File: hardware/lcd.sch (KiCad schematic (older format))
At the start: 3 parts

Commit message: Im Schaltplan die Debug LED mit Vorwiderstand durch einen PIN Header ersetz für eventuelle Erweiterung. Auf Revision 1.3 gesetzt
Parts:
- renumbered R11 to R10
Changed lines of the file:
@@
 Sheet 3 4
 Title "1541-rebuid"
-Date "2018-05-04"
-Rev "1.2.1"
+Date "2018-05-05"
+Rev "1.3"
 Comp ""
 Comment1 "Erstellt: von: Thorsten Kattanek"
@@
 	6850 3350 6850 3500
 $Comp
-L GND #PWR20
+L GND #PWR19
 U 1 1 55F9D0E8
 P 6850 3500
-F 0 "#PWR20" H 6850 3250 50  0001 C CNN
+F 0 "#PWR19" H 6850 3250 50  0001 C CNN
 F 1 "GND" H 6850 3350 50  0000 C CNN
 F 2 "" H 6850 3500 60  0000 C CNN
@@
 Connection ~ 5750 3400
 $Comp
-L +5V #PWR18
+L +5V #PWR17
 U 1 1 55F9F555
 P 5450 3500
-F 0 "#PWR18" H 5450 3350 50  0001 C CNN
+F 0 "#PWR17" H 5450 3350 50  0001 C CNN
 F 1 "+5V" H 5450 3640 50  0000 C CNN
 F 2 "" H 5450 3500 60  0000 C CNN
@@
 	5550 3750 5550 3350
 $Comp
-L +5V #PWR17
+L +5V #PWR16
 U 1 1 55F9F9A0
 P 4650 3400
-F 0 "#PWR17" H 4650 3250 50  0001 C CNN
+F 0 "#PWR16" H 4650 3250 50  0001 C CNN
 F 1 "+5V" H 4650 3540 50  0000 C CNN
 F 2 "" H 4650 3400 60  0000 C CNN
@@
 	4650 3400 4750 3400
 $Comp
-L R R11
+L R R10
 U 1 1 55F9FBFA
 P 6750 3850
-F 0 "R11" V 6830 3850 50  0000 C CNN
+F 0 "R10" V 6830 3850 50  0000 C CNN
 F 1 "150" V 6750 3850 50  0000 C CNN
 F 2 "Resistors_ThroughHole:Resistor_Horizontal_RM10mm" V 6680 3850 30  0001 C CNN
@@
 $EndComp
 $Comp
-L +5V #PWR19
+L +5V #PWR18
 U 1 1 55F9FC92
 P 6750 4100
-F 0 "#PWR19" H 6750 3950 50  0001 C CNN
+F 0 "#PWR18" H 6750 3950 50  0001 C CNN
 F 1 "+5V" H 6750 4240 50  0000 C CNN
 F 2 "" H 6750 4100 60  0000 C CNN

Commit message: LCD Display wird nun als 10 PIN Wannenstecker rausgeführt. PIN Belegung des Steckers wird im Schaltplan beschrieben.
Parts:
- removed DS1: LCD16X2, w_indicators:lcd_20x4, symbol LCD16X2
- added J2: LCD Display, symbol Conn_02x05_Odd_Even
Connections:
- wire segments 23 -> 16
- no-connect marks 4 -> 0
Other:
- note added: "R10 hängt von der Hintergrundbeleuchtung des LCD Displays ab !"
- note added: "Steckerbelegung für das LCD Display (20x4)\n\nPIN_01: VDD(2) ... +5V\nPIN_02: VSS(1), R/W(5), LED-/K(16) ... GND\nPIN_03: D4(11)\nPIN_04: D5(12)\nPIN_05: D6(13)\nPIN_06: D7(14)\nPIN_07: E(6)\nPIN_08: RS(4)\nPIN_09: LED+/A(15)\nPIN_10: VO(3)\n"
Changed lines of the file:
@@
 Title "1541-rebuid"
 Date "2018-05-05"
-Rev "1.3"
+Rev "1.3.1"
 Comp ""
 Comment1 "Erstellt: von: Thorsten Kattanek"
@@
 Comment4 ""
 $EndDescr
-Text HLabel 4700 4000 0    60   Input ~ 0
-D0
-Text HLabel 4700 4100 0    60   Input ~ 0
-D1
-Text HLabel 4700 4200 0    60   Input ~ 0
-D2
-Text HLabel 4700 4300 0    60   Input ~ 0
-D3
-Text HLabel 4700 3800 0    60   Input ~ 0
-RS
-Text HLabel 4700 3900 0    60   Input ~ 0
-EN
-NoConn ~ 5950 3350
-NoConn ~ 6050 3350
-NoConn ~ 6150 3350
-NoConn ~ 6250 3350
-Wire Wire Line
-	4700 4000 6350 4000
-Wire Wire Line
-	6350 4000 6350 3350
-Wire Wire Line
-	4700 4100 6450 4100
-Wire Wire Line
-	6450 4100 6450 3350
-Wire Wire Line
-	4700 4200 6550 4200
-Wire Wire Line
-	6550 4200 6550 3350
-Wire Wire Line
-	4700 4300 6650 4300
-Wire Wire Line
-	6650 4300 6650 3350
-Wire Wire Line
-	4700 3900 5850 3900
-Wire Wire Line
-	5850 3900 5850 3350
-Wire Wire Line
-	4700 3800 5650 3800
-Wire Wire Line
-	5650 3800 5650 3350
-Wire Wire Line
-	5750 3350 5750 3400
-Wire Wire Line
-	5250 3400 6850 3400
-Wire Wire Line
-	6850 3350 6850 3500
 $Comp
-L GND #PWR19
-U 1 1 55F9D0E8
-P 6850 3500
-F 0 "#PWR19" H 6850 3250 50  0001 C CNN
-F 1 "GND" H 6850 3350 50  0000 C CNN
-F 2 "" H 6850 3500 60  0000 C CNN
-F 3 "" H 6850 3500 60  0000 C CNN
-	1    6850 3500
+L Conn_02x05_Odd_Even J2
+U 1 1 5AEE2FA0
+P 5050 3600
+F 0 "J2" H 5100 3900 50  0000 C CNN
+F 1 "LCD Display" H 5100 3300 50  0000 C CNN
+F 2 "" H 5050 3600 50  0001 C CNN
+F 3 "" H 5050 3600 50  0001 C CNN
+	1    5050 3600
+	0    1    1    0
+$EndComp
+Text Notes 5950 4100 0    60   ~ 0
+Steckerbelegung für das LCD Display (20x4)\n\nPIN_01: VDD(2) ... +5V\nPIN_02: VSS(1), R/W(5), LED-/K(16) ... GND\nPIN_03: D4(11)\nPIN_04: D5(12)\nPIN_05: D6(13)\nPIN_06: D7(14)\nPIN_07: E(6)\nPIN_08: RS(4)\nPIN_09: LED+/A(15)\nPIN_10: VO(3)\n
+$Comp
+L +5V #PWR17
+U 1 1 5AEE3573
+P 5250 2450
+F 0 "#PWR17" H 5250 2300 50  0001 C CNN
+F 1 "+5V" H 5250 2590 50  0000 C CNN
+F 2 "" H 5250 2450 60  0000 C CNN
+F 3 "" H 5250 2450 60  0000 C CNN
+	1    5250 2450
 	1    0    0    -1
 $EndComp
-Connection ~ 6850 3400
+Text HLabel 5150 2900 1    60   Input ~ 0
+D0
+Text HLabel 5150 4150 3    60   Input ~ 0
+D1
+Text HLabel 5050 2900 1    60   Input ~ 0
+D2
+Text HLabel 5050 4150 3    60   Input ~ 0
+D3
+Text HLabel 4950 2900 1    60   Input ~ 0
+EN
+Text HLabel 4950 4150 3    60   Input ~ 0
+RS
+Wire Wire Line
+	5250 2450 5250 2550
+Wire Wire Line
+	5250 2550 5250 3400
+Wire Wire Line
+	5150 2900 5150 3400
+Wire Wire Line
+	5150 3900 5150 4150
+Wire Wire Line
+	5050 3400 5050 2900
+Wire Wire Line
+	5050 3900 5050 4150
+Wire Wire Line
+	4950 2900 4950 3400
+Wire Wire Line
+	4950 3900 4950 4150
 $Comp
-L LCD16X2 DS1
-U 1 1 55F9CFCD
-P 6100 2850
-F 0 "DS1" H 5300 3250 40  0000 C CNN
-F 1 "LCD16X2" H 6800 3250 40  0000 C CNN
-F 2 "w_indicators:lcd_20x4" H 6100 2800 35  0000 C CIN
-F 3 "" H 6100 2850 60  0000 C CNN
-	1    6100 2850
+L R R10
+U 1 1 5AEE40E3
+P 4850 3100
+F 0 "R10" V 4930 3100 50  0000 C CNN
+F 1 "150" V 4850 3100 50  0000 C CNN
+F 2 "Resistors_ThroughHole:Resistor_Horizontal_RM10mm" V 4780 3100 30  0001 C CNN
+F 3 "" H 4850 3100 30  0000 C CNN
+	1    4850 3100
+	-1   0    0    1
+$EndComp
+Wire Wire Line
+	4850 2950 4850 2550
+Wire Wire Line
+	4850 2550 5250 2550
+Connection ~ 5250 2550
+Wire Wire Line
+	4850 3250 4850 3400
+$Comp
+L GND #PWR18
+U 1 1 5AEE45C6
+P 5250 4750
+F 0 "#PWR18" H 5250 4500 50  0001 C CNN
+F 1 "GND" H 5250 4600 50  0000 C CNN
+F 2 "" H 5250 4750 60  0000 C CNN
+F 3 "" H 5250 4750 60  0000 C CNN
+	1    5250 4750
 	1    0    0    -1
 $EndComp
 Wire Wire Line
-	5350 3350 5350 3400
-Connection ~ 5750 3400
+	5250 3900 5250 4550
+Wire Wire Line
+	5250 4550 5250 4750
 $Comp
-L +5V #PWR17
-U 1 1 55F9F555
-P 5450 3500
-F 0 "#PWR17" H 5450 3350 50  0001 C CNN
-F 1 "+5V" H 5450 3640 50  0000 C CNN
-F 2 "" H 5450 3500 60  0000 C CNN
-F 3 "" H 5450 3500 60  0000 C CNN
-	1    5450 3500
-	-1   0    0    1
+L POT-RESCUE-1541-rebuild RV1
+U 1 1 5AEE481D
+P 4850 4550
+F 0 "RV1" H 4850 4450 50  0000 C CNN
+F 1 "10k" H 4850 4550 50  0000 C CNN
+F 2 "Potentiometers:Potentiometer_Bourns_3339P_Angular_ScrewUp" H 4850 4550 60  0001 C CNN
+F 3 "" H 4850 4550 60  0000 C CNN
+	1    4850 4550
+	1    0    0    -1
 $EndComp
 Wire Wire Line
-	5450 3350 5450 3500
-$Comp
-L POT-RESCUE-1541-rebuild RV1
-U 1 1 55F9F8C0
-P 5000 3400
-F 0 "RV1" H 5000 3300 50  0000 C CNN
-F 1 "10k" H 5000 3400 50  0000 C CNN
-F 2 "Potentiometers:Potentiometer_Bourns_3339P_Angular_ScrewUp" H 5000 3400 60  0001 C CNN
-F 3 "" H 5000 3400 60  0000 C CNN
-	1    5000 3400
-	-1   0    0    1
-$EndComp
-Connection ~ 5350 3400
+	5100 4550 5250 4550
+Connection ~ 5250 4550
 Wire Wire Line
-	5000 3550 5000 3750
-Wire Wire Line
-	5000 3750 5550 3750
-Wire Wire Line
-	5550 3750 5550 3350
+	4850 3900 4850 4400
 $Comp
 L +5V #PWR16
-U 1 1 55F9F9A0
-P 4650 3400
-F 0 "#PWR16" H 4650 3250 50  0001 C CNN
-F 1 "+5V" H 4650 3540 50  0000 C CNN
-F 2 "" H 4650 3400 60  0000 C CNN
-F 3 "" H 4650 3400 60  0000 C CNN
-	1    4650 3400
+U 1 1 5AEE4960
+P 4350 4550
+F 0 "#PWR16" H 4350 4400 50  0001 C CNN
+F 1 "+5V" H 4350 4690 50  0000 C CNN
+F 2 "" H 4350 4550 60  0000 C CNN
+F 3 "" H 4350 4550 60  0000 C CNN
+	1    4350 4550
 	0    -1   -1   0
 $EndComp
 Wire Wire Line
-	4650 3400 4750 3400
-$Comp
-L R R10
-U 1 1 55F9FBFA
-P 6750 3850
-F 0 "R10" V 6830 3850 50  0000 C CNN
-F 1 "150" V 6750 3850 50  0000 C CNN
-F 2 "Resistors_ThroughHole:Resistor_Horizontal_RM10mm" V 6680 3850 30  0001 C CNN
-F 3 "" H 6750 3850 30  0000 C CNN
-	1    6750 3850
-	1    0    0    -1
-$EndComp
-$Comp
-L +5V #PWR18
-U 1 1 55F9FC92
-P 6750 4100
-F 0 "#PWR18" H 6750 3950 50  0001 C CNN
-F 1 "+5V" H 6750 4240 50  0000 C CNN
-F 2 "" H 6750 4100 60  0000 C CNN
-F 3 "" H 6750 4100 60  0000 C CNN
-	1    6750 4100
-	-1   0    0    1
-$EndComp
-Wire Wire Line
-	6750 3350 6750 3700
-Wire Wire Line
-	6750 4000 6750 4100
+	4350 4550 4600 4550
+Text Notes 650  7600 0    60   ~ 0
+R10 hängt von der Hintergrundbeleuchtung des LCD Displays ab !
 $EndSCHEMATC

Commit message: Im Schaltplan die 3 Steuertasten als 4 PINS (Key1, Key2, Key3 und GND) rausgeführt. Auf Revesion 1.3.2 gesetzt.
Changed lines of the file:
@@
 Sheet 3 4
 Title "1541-rebuid"
-Date "2018-05-05"
-Rev "1.3.1"
+Date "2018-05-06"
+Rev "1.3.2"
 Comp ""
 Comment1 "Erstellt: von: Thorsten Kattanek"
@@
 RS
 Wire Wire Line
-	5250 2450 5250 2550
-Wire Wire Line
-	5250 2550 5250 3400
+	5250 2450 5250 3400
 Wire Wire Line
 	5150 2900 5150 3400
@@
 $EndComp
 Wire Wire Line
-	5250 3900 5250 4550
-Wire Wire Line
-	5250 4550 5250 4750
+	5250 3900 5250 4750
 $Comp
 L POT-RESCUE-1541-rebuild RV1

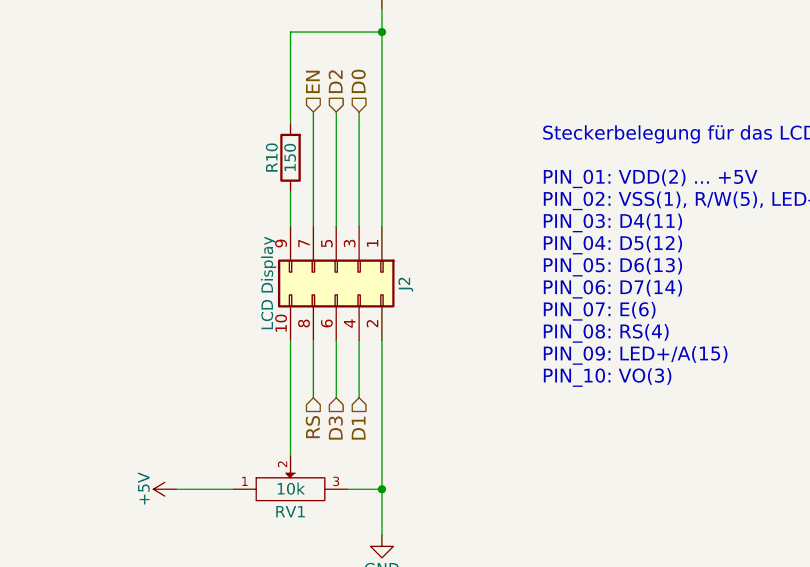
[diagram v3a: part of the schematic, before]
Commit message: Jumper für EXT_5V hinzugefügt. Schaltplan aufgeräumt. Schaltplan auf Revision 1.3.3 gesetzt.
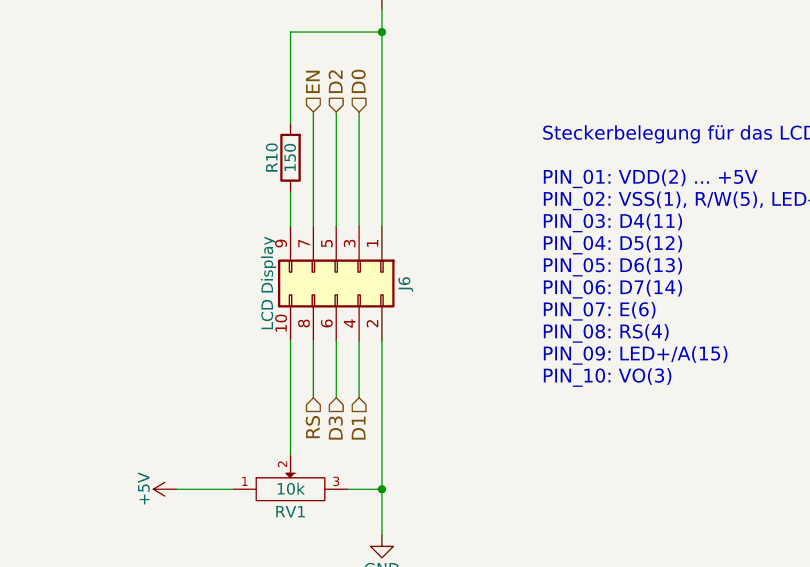
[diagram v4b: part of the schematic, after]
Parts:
- renumbered J2 to J6
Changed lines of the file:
@@
 Title "1541-rebuid"
 Date "2018-05-06"
-Rev "1.3.2"
+Rev "1.3.3"
 Comp ""
 Comment1 "Erstellt: von: Thorsten Kattanek"
@@
 $EndDescr
 $Comp
-L Conn_02x05_Odd_Even J2
+L Conn_02x05_Odd_Even J6
 U 1 1 5AEE2FA0
 P 5050 3600
-F 0 "J2" H 5100 3900 50  0000 C CNN
+F 0 "J6" H 5100 3900 50  0000 C CNN
 F 1 "LCD Display" H 5100 3300 50  0000 C CNN
 F 2 "" H 5050 3600 50  0001 C CNN
@@
 Steckerbelegung für das LCD Display (20x4)\n\nPIN_01: VDD(2) ... +5V\nPIN_02: VSS(1), R/W(5), LED-/K(16) ... GND\nPIN_03: D4(11)\nPIN_04: D5(12)\nPIN_05: D6(13)\nPIN_06: D7(14)\nPIN_07: E(6)\nPIN_08: RS(4)\nPIN_09: LED+/A(15)\nPIN_10: VO(3)\n
 $Comp
-L +5V #PWR17
+L +5V #PWR18
 U 1 1 5AEE3573
 P 5250 2450
-F 0 "#PWR17" H 5250 2300 50  0001 C CNN
+F 0 "#PWR18" H 5250 2300 50  0001 C CNN
 F 1 "+5V" H 5250 2590 50  0000 C CNN
 F 2 "" H 5250 2450 60  0000 C CNN
@@
 	4850 3250 4850 3400
 $Comp
-L GND #PWR18
+L GND #PWR20
 U 1 1 5AEE45C6
 P 5250 4750
-F 0 "#PWR18" H 5250 4500 50  0001 C CNN
+F 0 "#PWR20" H 5250 4500 50  0001 C CNN
 F 1 "GND" H 5250 4600 50  0000 C CNN
 F 2 "" H 5250 4750 60  0000 C CNN
@@
 	4850 3900 4850 4400
 $Comp
-L +5V #PWR16
+L +5V #PWR19
 U 1 1 5AEE4960
 P 4350 4550
-F 0 "#PWR16" H 4350 4400 50  0001 C CNN
+F 0 "#PWR19" H 4350 4400 50  0001 C CNN
 F 1 "+5V" H 4350 4690 50  0000 C CNN
 F 2 "" H 4350 4550 60  0000 C CNN

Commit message: Allen Bauteilen Footprints zugeordnet.
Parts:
- J6: footprint (none) -> w_conn_strip:vasch_strip_5x2
- R10: footprint Resistors_ThroughHole:Resistor_Horizontal_RM10mm -> Discret:R4-5
- RV1: footprint Potentiometers:Potentiometer_Bourns_3339P_Angular_ScrewUp -> w_pth_resistors:trimmer_vishay_64w
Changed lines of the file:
@@
 F 0 "J6" H 5100 3900 50  0000 C CNN
 F 1 "LCD Display" H 5100 3300 50  0000 C CNN
-F 2 "" H 5050 3600 50  0001 C CNN
+F 2 "w_conn_strip:vasch_strip_5x2" H 5050 3600 50  0001 C CNN
 F 3 "" H 5050 3600 50  0001 C CNN
 	1    5050 3600
@@
 F 0 "R10" V 4930 3100 50  0000 C CNN
 F 1 "150" V 4850 3100 50  0000 C CNN
-F 2 "Resistors_ThroughHole:Resistor_Horizontal_RM10mm" V 4780 3100 30  0001 C CNN
+F 2 "Discret:R4-5" V 4780 3100 30  0001 C CNN
 F 3 "" H 4850 3100 30  0000 C CNN
 	1    4850 3100
@@
 F 0 "RV1" H 4850 4450 50  0000 C CNN
 F 1 "10k" H 4850 4550 50  0000 C CNN
-F 2 "Potentiometers:Potentiometer_Bourns_3339P_Angular_ScrewUp" H 4850 4550 60  0001 C CNN
+F 2 "w_pth_resistors:trimmer_vishay_64w" H 4850 4550 60  0001 C CNN
 F 3 "" H 4850 4550 60  0000 C CNN
 	1    4850 4550
